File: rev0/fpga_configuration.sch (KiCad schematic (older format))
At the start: 41 parts, among them IC1 ECP5-BGA256, J10 TC_SWD, J5 Conn_FPGA_JTAG_10, J6 Conn_ARM_JTAG_SWD_10, U6 ATSAMD11D14A-MUT, U7 W25Q32JVSS

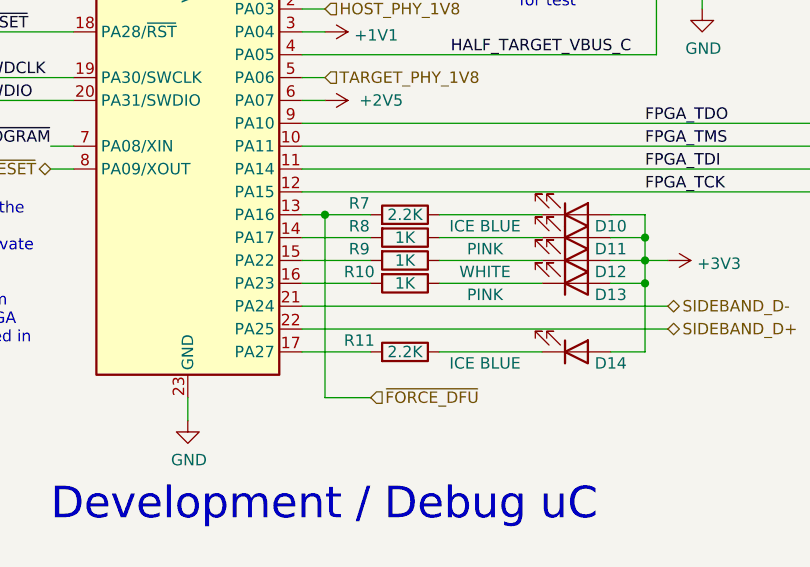
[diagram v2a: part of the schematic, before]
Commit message: hardware: reduce LED brightness
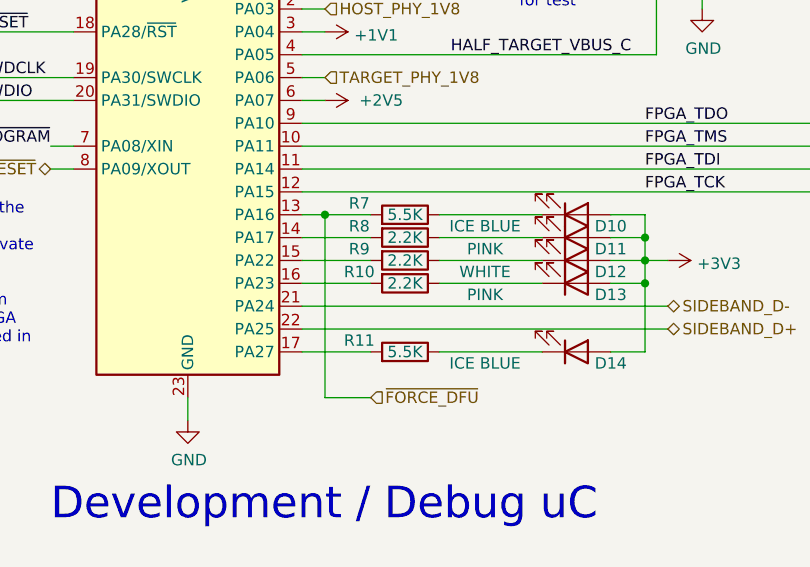
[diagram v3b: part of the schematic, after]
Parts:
- R10, R8, R9: value 1K -> 2.2K; Part Number GENERIC-RES-0402-1K -> GENERIC-RES-0402-2.2K
- R11, R7: value 2.2K -> 5.5K; Description (none) -> RES SMD 5.49K OHM 1% 1/10W 0402; Manufacturer (none) -> Panasonic; Part Number GENERIC-RES-0402-2.2K -> ERJ-2RKF5491X
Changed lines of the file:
@@
 AR Path="/5DCAA6D2/5FFED8BB" Ref="R8"  Part="1"
 F 0 "R8" V 4550 3250 50  0000 C CNN
-F 1 "1K" V 4600 3450 50  0000 C CNN
+F 1 "2.2K" V 4600 3450 50  0000 C CNN
 F 2 "Resistor_SMD:R_0402_1005Metric" V 4530 3450 50  0001 C CNN
 F 3 "~" H 4600 3450 50  0001 C CNN
-F 4 "GENERIC-RES-0402-1K" H 4600 3450 50  0001 C CNN "Part Number"
+F 4 "GENERIC-RES-0402-2.2K" H 4600 3450 50  0001 C CNN "Part Number"
 F 5 "any equivalent" H 4600 3450 50  0001 C CNN "Substitution"
 	1    4600 3450
@@
 AR Path="/5DCAA6D2/60003542" Ref="R9"  Part="1"
 F 0 "R9" V 4550 3350 50  0000 C CNN
-F 1 "1K" V 4600 3550 50  0000 C CNN
+F 1 "2.2K" V 4600 3550 50  0000 C CNN
 F 2 "Resistor_SMD:R_0402_1005Metric" V 4530 3550 50  0001 C CNN
 F 3 "~" H 4600 3550 50  0001 C CNN
-F 4 "GENERIC-RES-0402-1K" H 4600 3550 50  0001 C CNN "Part Number"
+F 4 "GENERIC-RES-0402-2.2K" H 4600 3550 50  0001 C CNN "Part Number"
 F 5 "any equivalent" H 4600 3550 50  0001 C CNN "Substitution"
 	1    4600 3550
@@
 AR Path="/5DCAA6D2/60003831" Ref="R10"  Part="1"
 F 0 "R10" V 4550 3450 50  0000 C CNN
-F 1 "1K" V 4600 3650 50  0000 C CNN
+F 1 "2.2K" V 4600 3650 50  0000 C CNN
 F 2 "Resistor_SMD:R_0402_1005Metric" V 4530 3650 50  0001 C CNN
 F 3 "~" H 4600 3650 50  0001 C CNN
-F 4 "GENERIC-RES-0402-1K" H 4600 3650 50  0001 C CNN "Part Number"
+F 4 "GENERIC-RES-0402-2.2K" H 4600 3650 50  0001 C CNN "Part Number"
 F 5 "any equivalent" H 4600 3650 50  0001 C CNN "Substitution"
 	1    4600 3650
@@
 AR Path="/5DCAA6D2/6001DCF6" Ref="R7"  Part="1"
 F 0 "R7" V 4650 3150 50  0000 C CNN
-F 1 "2.2K" V 4600 3350 50  0000 C CNN
+F 1 "5.5K" V 4600 3350 50  0000 C CNN
 F 2 "Resistor_SMD:R_0402_1005Metric" V 4530 3350 50  0001 C CNN
 F 3 "~" H 4600 3350 50  0001 C CNN
-F 4 "GENERIC-RES-0402-2.2K" H 4600 3350 50  0001 C CNN "Part Number"
+F 4 "ERJ-2RKF5491X" H 4600 3350 50  0001 C CNN "Part Number"
 F 5 "any equivalent" H 4600 3350 50  0001 C CNN "Substitution"
+F 6 "RES SMD 5.49K OHM 1% 1/10W 0402" H 4600 3350 50  0001 C CNN "Description"
+F 7 "Panasonic" H 4600 3350 50  0001 C CNN "Manufacturer"
 	1    4600 3350
 	0    1    -1   0
@@
 AR Path="/5DCAA6D2/6002A83C" Ref="R11"  Part="1"
 F 0 "R11" V 4650 3750 50  0000 C CNN
-F 1 "2.2K" V 4600 3950 50  0000 C CNN
+F 1 "5.5K" V 4600 3950 50  0000 C CNN
 F 2 "Resistor_SMD:R_0402_1005Metric" V 4530 3950 50  0001 C CNN
 F 3 "~" H 4600 3950 50  0001 C CNN
-F 4 "GENERIC-RES-0402-2.2K" H 4600 3950 50  0001 C CNN "Part Number"
+F 4 "ERJ-2RKF5491X" H 4600 3950 50  0001 C CNN "Part Number"
 F 5 "any equivalent" H 4600 3950 50  0001 C CNN "Substitution"
+F 6 "RES SMD 5.49K OHM 1% 1/10W 0402" H 4600 3950 50  0001 C CNN "Description"
+F 7 "Panasonic" H 4600 3950 50  0001 C CNN "Manufacturer"
 	1    4600 3950
 	0    1    -1   0

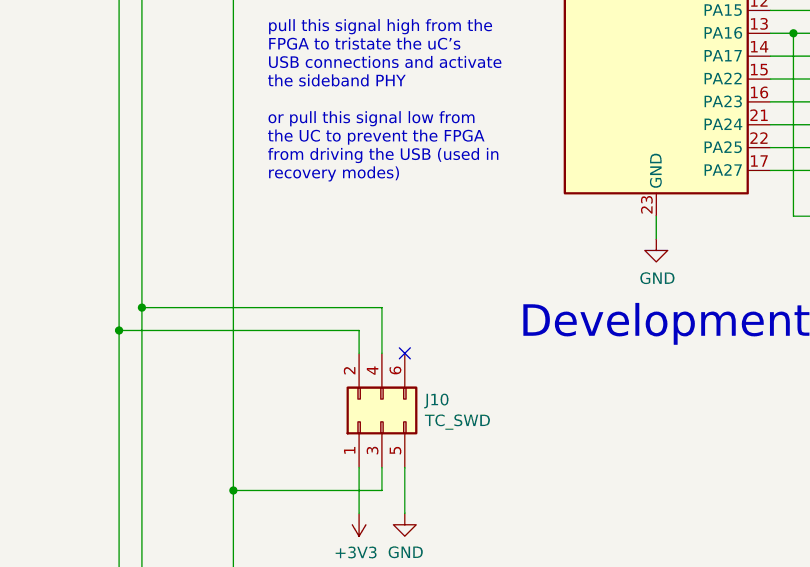
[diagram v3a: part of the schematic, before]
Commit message: hardware: add ability to power board via J10
- add diode to take 5 V input from J10 (Tag-Connect) pin 6
- add TC2030-CTX as an alternative part for J10
- move reset trace away from board edge
- minor track and via adjustments
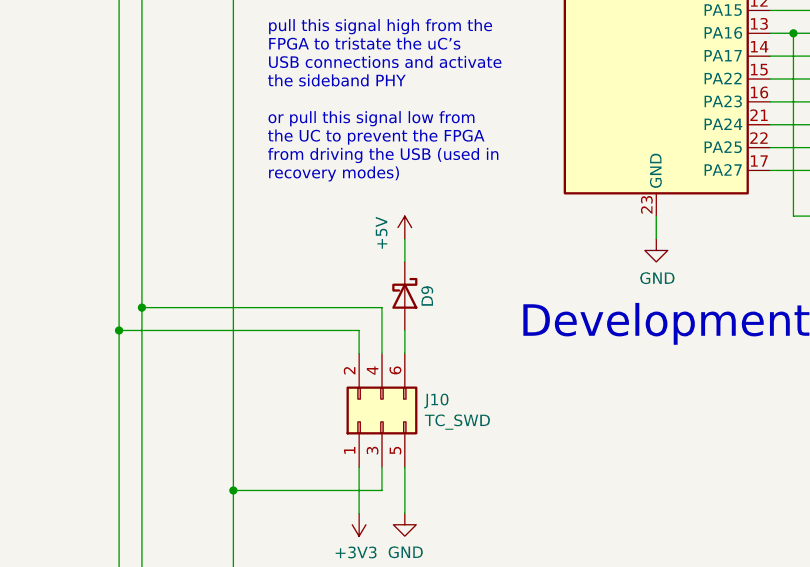
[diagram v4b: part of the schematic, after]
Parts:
- added D9: PMEG4010ESBYL, Diode_SMD:D_0402_1005Metric, symbol Device:D_Schottky
- J10: Substitution (none) -> TC2030-CTX
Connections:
- net at J10.6 (Pin_6): now also D9.2 (A)
- new net +5V: D9.1 (K)
- no-connect marks 12 -> 11
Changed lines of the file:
@@
 	-1   0    0    -1
 $EndComp
-NoConn ~ 2550 4750
 $Comp
 L power:GND #PWR0131
@@
 F 5 "DNP" H 2450 5050 50  0001 C CNN "Note"
 F 6 "TC2030-IDC" H 2450 5050 50  0001 C CNN "Part Number"
+F 7 "TC2030-CTX" H 2450 5050 50  0001 C CNN "Substitution"
 	1    2450 5050
 	0    -1   -1   0
@@
 	0    1    -1   0
 $EndComp
+$Comp
+L power:+5V #PWR?
+U 1 1 604E0BAD
+P 2550 4250
+AR Path="/604E0BAD" Ref="#PWR?"  Part="1"
+AR Path="/5DCAA6D2/604E0BAD" Ref="#PWR0136"  Part="1"
+F 0 "#PWR0136" H 2550 4100 50  0001 C CNN
+F 1 "+5V" V 2450 4200 50  0000 L CNN
+F 2 "" H 2550 4250 50  0001 C CNN
+F 3 "" H 2550 4250 50  0001 C CNN
+	1    2550 4250
+	1    0    0    -1
+$EndComp
+$Comp
+L Device:D_Schottky D?
+U 1 1 604E0BB6
+P 2550 4500
+AR Path="/604E0BB6" Ref="D?"  Part="1"
+AR Path="/5DCAA6D2/604E0BB6" Ref="D9"  Part="1"
+F 0 "D9" H 2550 4600 50  0000 C CNN
+F 1 "PMEG4010ESBYL" H 2450 4650 50  0001 C CNN
+F 2 "Diode_SMD:D_0402_1005Metric" H 2550 4500 50  0001 C CNN
+F 3 "~" H 2550 4500 50  0001 C CNN
+F 4 "Nexperia" H 2550 4500 50  0001 C CNN "Manufacturer"
+F 5 "PMEG4010ESBYL" H 2550 4500 50  0001 C CNN "Part Number"
+F 6 "DIODE SCHOTTKY 40V 1A DSN1006-2" H 2550 4500 50  0001 C CNN "Description"
+	1    2550 4500
+	0    1    1    0
+$EndComp
+Wire Wire Line
+	2550 4250 2550 4350
+Wire Wire Line
+	2550 4750 2550 4650
 $EndSCHEMATC

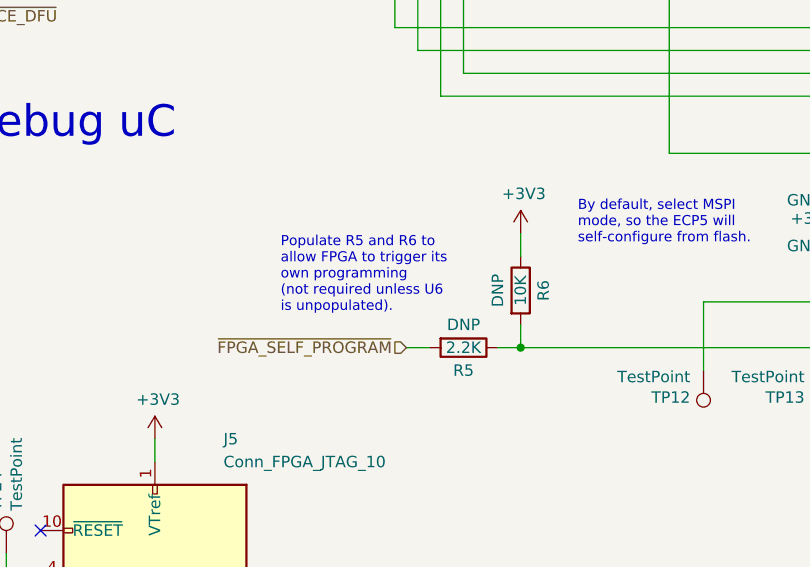
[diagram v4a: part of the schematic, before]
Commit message: hardware: populate FPGA self-programming resistors
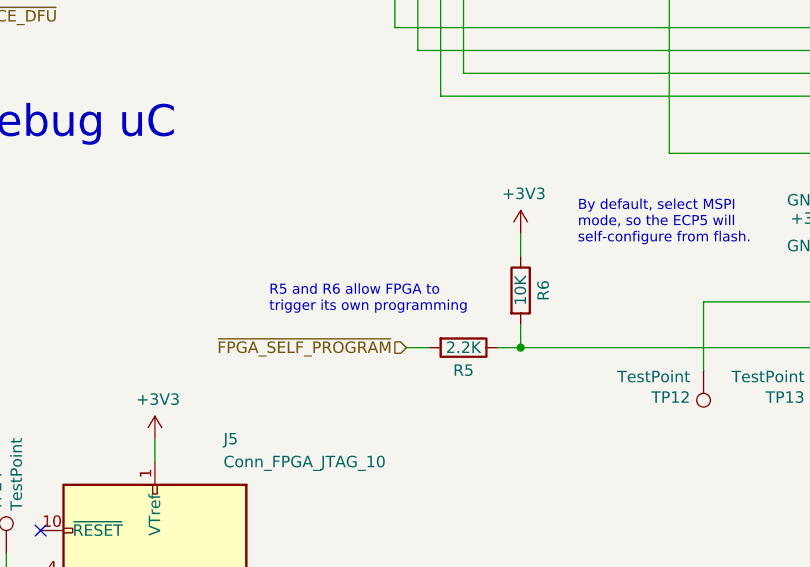
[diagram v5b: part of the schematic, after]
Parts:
- R5, R6: Note DNP -> (none)
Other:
- note added: "R5 and R6 allow FPGA to\ntrigger its own programming"
- note removed: "Populate R5 and R6 to\nallow FPGA to trigger its\nown programming\n(not required unless U6\nis unpopulated)."
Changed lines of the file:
@@
 F 3 "~" H 6950 5350 50  0001 C CNN
 F 4 "GENERIC-RES-0402-10K" H 6950 5350 50  0001 C CNN "Part Number"
-F 5 "DNP" V 6850 5350 50  0000 C CNN "Note"
-F 6 "any equivalent" H 6950 5350 50  0001 C CNN "Substitution"
+F 5 "any equivalent" H 6950 5350 50  0001 C CNN "Substitution"
 	1    6950 5350
 	1    0    0    -1
@@
 F 3 "~" H 6700 5600 50  0001 C CNN
 F 4 "GENERIC-RES-0402-2.2K" H 6700 5600 50  0001 C CNN "Part Number"
-F 5 "DNP" V 6600 5600 50  0000 C CNN "Note"
-F 6 "any equivalent" H 6700 5600 50  0001 C CNN "Substitution"
+F 5 "any equivalent" H 6700 5600 50  0001 C CNN "Substitution"
 	1    6700 5600
 	0    1    1    0
 $EndComp
-Text Notes 5900 5450 0    44   ~ 0
-Populate R5 and R6 to\nallow FPGA to trigger its\nown programming\n(not required unless U6\nis unpopulated).
+Text Notes 5850 5450 0    44   ~ 0
+R5 and R6 allow FPGA to\ntrigger its own programming
 Text HLabel 6450 5600 0    50   Input ~ 0
 ~FPGA_SELF_PROGRAM

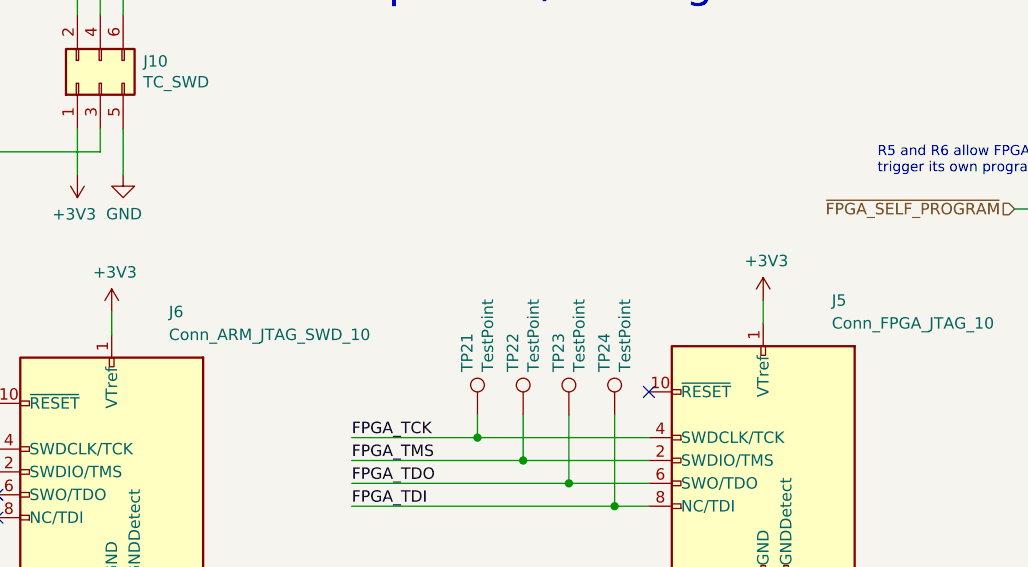
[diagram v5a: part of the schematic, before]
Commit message: hardware: do not populate J5, J6
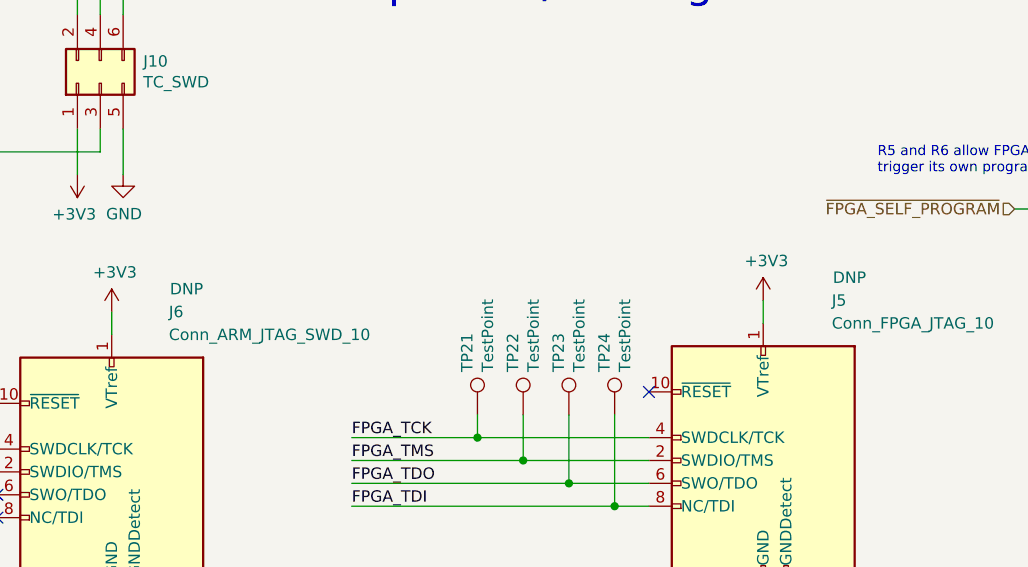
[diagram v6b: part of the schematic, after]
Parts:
- J5, J6: Note (none) -> DNP
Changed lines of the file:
@@
 F 5 "Samtec" H 2500 6750 50  0001 C CNN "Manufacturer"
 F 6 "FTSH-105-01-F-D-K" H 2500 6750 50  0001 C CNN "Part Number"
+F 7 "DNP" H 2100 7550 50  0000 L CNN "Note"
 	1    2500 6750
 	-1   0    0    -1
@@
 F 5 "Samtec" H 5350 6700 50  0001 C CNN "Manufacturer"
 F 6 "FTSH-105-01-F-D-K" H 5350 6700 50  0001 C CNN "Part Number"
+F 7 "DNP" H 4900 7500 50  0000 L CNN "Note"
 	1    5350 6700
 	-1   0    0    -1

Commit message: hardware: add ATSAMD11D14A-MNT substitution for U6
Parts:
- U6: Substitution (none) -> ATSAMD11D14A-MNT
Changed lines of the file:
@@
 F 5 "Microchip" H 3650 3150 50  0001 C CNN "Manufacturer"
 F 6 "ATSAMD11D14A-MUT" H 3650 3150 50  0001 C CNN "Part Number"
+F 7 "ATSAMD11D14A-MNT" H 3650 3150 50  0001 C CNN "Substitution"
 	1    3650 3150
 	1    0    0    -1
